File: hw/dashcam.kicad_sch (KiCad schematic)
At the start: 1 part, among them U1 AM6254ATCGHAALW

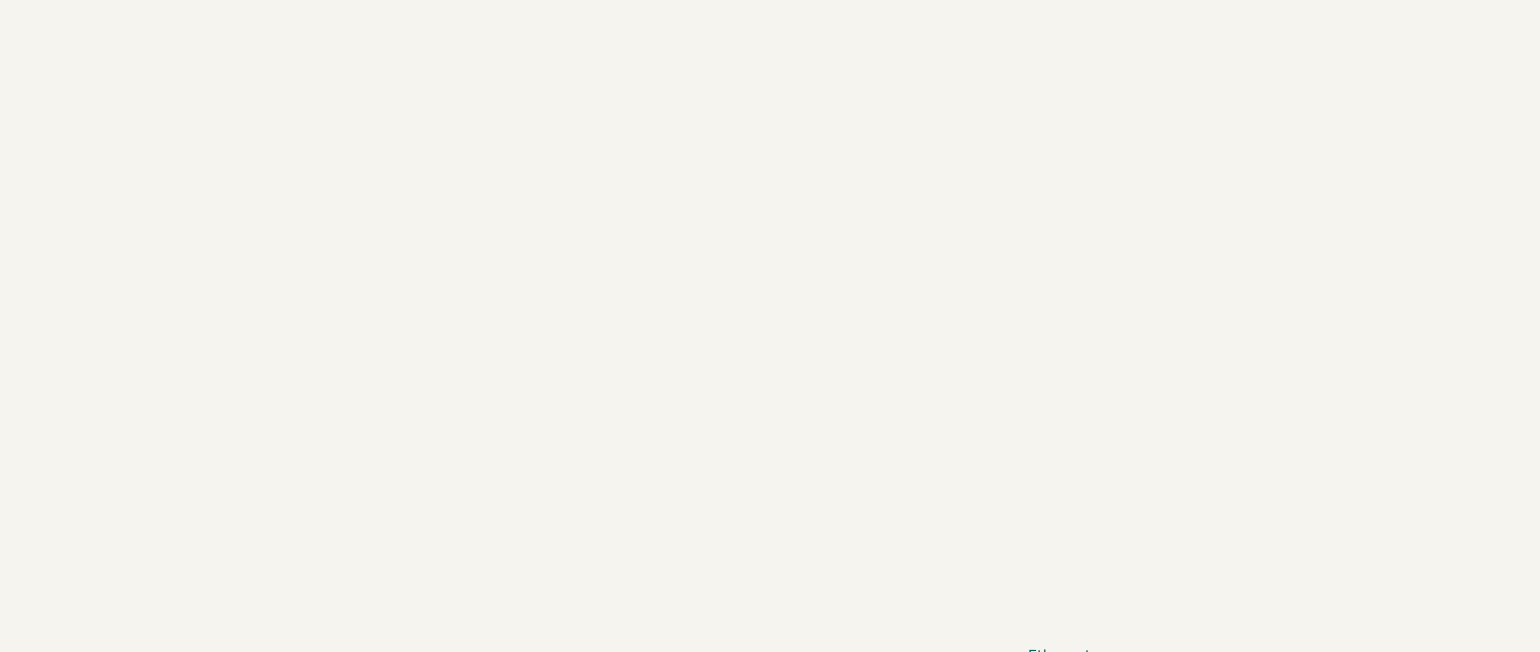
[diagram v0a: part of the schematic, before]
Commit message: Folder rest. and rtc design with OSC yet to be connected
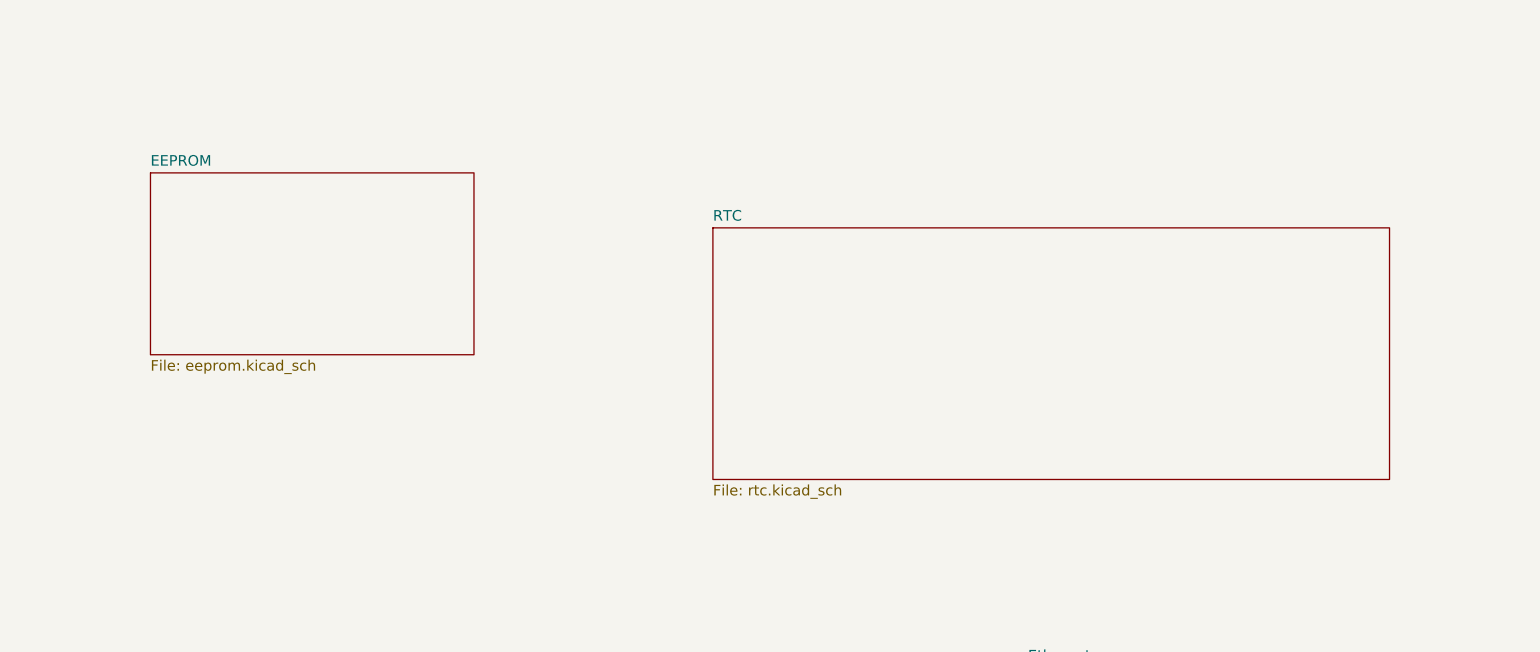
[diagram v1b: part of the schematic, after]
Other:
- added sheet EEPROM (eeprom.kicad_sch)
- added sheet RTC (rtc.kicad_sch)
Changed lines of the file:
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@@
+	)
+	(sheet
+		(at 245.364 99.568)
+		(size 81.28 30.226)
+		(exclude_from_sim no)
+		(in_bom yes)
+		(on_board yes)
+		(dnp no)
+		(fields_autoplaced yes)
+		(stroke
+			(width 0.1524)
+			(type solid)
+		)
+		(fill
+			(color 0 0 0 0.0000)
+		)
+		(property "Sheetname" "RTC"
+			(at 245.364 98.8564 0)
+			(effects
+				(font
+					(size 1.27 1.27)
+				)
+				(justify left bottom)
+			)
+		)
+		(property "Sheetfile" "rtc.kicad_sch"
+			(at 245.364 130.3786 0)
+			(effects
+				(font
+					(size 1.27 1.27)
+				)
+				(justify left top)
+			)
+		)
+		(instances
+			(project "dashcam"
+				(path "/30d6913c-7aa4-4f56-9882-2ba08f7e2cce"
+					(page "15")
+				)
+			)
+		)
 	)
 	(sheet
@@
 				)
 			)
+		)
+	)
+	(sheet
+		(at 177.8 92.964)
+		(size 38.862 21.844)
+		(exclude_from_sim no)
+		(in_bom yes)
+		(on_board yes)
+		(dnp no)
+		(fields_autoplaced yes)
+		(stroke
+			(width 0.1524)
+			(type solid)
+		)
+		(fill
+			(color 0 0 0 0.0000)
+		)
+		(property "Sheetname" "EEPROM"
+			(at 177.8 92.2524 0)
+			(effects
+				(font
+					(size 1.27 1.27)
+				)
+				(justify left bottom)
+			)
+		)
+		(property "Sheetfile" "eeprom.kicad_sch"
+			(at 177.8 115.3926 0)
+			(effects
+				(font
+					(size 1.27 1.27)
+				)
+				(justify left top)
+			)
+		)
+		(instances
+			(project "dashcam"
+				(path "/30d6913c-7aa4-4f56-9882-2ba08f7e2cce"
+					(page "13")
+				)
+			)

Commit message: Ethernet...
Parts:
- removed unit 6 of U1
- added X2: SC-20S32.768kHz20PPM9pF, pepy_sym_lib:[Crystal]Seiko SC-20S,32.768kHz,20PPM,9pF, symbol pepy_sym_lib:[Crystal]Seiko SC-20S,32.768kHz,20PPM,9pF
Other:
- added sheet LTE (LTE.kicad_sch)
- added sheet ddr (ddr.kicad_sch)

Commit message: WIP SIM module
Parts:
- added R1: RC0201FR-0733RL, pepy_sym_lib:[RES_SMD_0201_0603Metric], symbol pepy_sym_lib:[RES_SMD_0201_0603Metric]YAGEO RC0201FR-0733RL
- renumbered X2 to X1
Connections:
- net at U1.B8 (MCU_SPI0_CS1): now also R1.1
- new net MCU_OBSCLK0: R1.2
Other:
- note added: "CLK to PHY (25MHz) [MCU Domain Observation clock output for test and debug purposes only]"
- moved on the sheet: U1R
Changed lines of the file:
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@@
 		(rev "v0.1")
 	)
+	(text "CLK to PHY (25MHz) [MCU Domain Observation clock\noutput for test and debug purposes only]"
+		(exclude_from_sim no)
+		(at 163.83 44.704 0)
+		(effects
+			(font
+				(size 0.6 0.6)
+			)
+			(justify left)
+		)
+	)
 	(no_connect
 		(at 558.8 -191.77)
@@
 		(at 558.8 -194.31)
 	)
+	(wire
+		(pts
+			(xy 143.51 44.45) (xy 147.32 44.45)
+		)
+		(stroke
+			(width 0)
+			(type default)
+		)
+	)
+	(wire
+		(pts
+			(xy 138.43 44.45) (xy 137.16 44.45)
+		)
+		(stroke
+			(width 0)
+			(type default)
+		)
+	)
+	(global_label "MCU_OBSCLK0"
+		(shape output)
+		(at 147.32 44.45 0)
+		(fields_autoplaced yes)
+		(effects
+			(font
+				(size 1.27 1.27)
+			)
+			(justify left)
+		)
+		(property "Intersheetrefs" "${INTERSHEET_REFS}"
+			(at 163.9123 44.45 0)
+			(effects
+				(font
+					(size 1.27 1.27)
+				)
+				(justify left)
+				(hide yes)
+			)
+		)
+	)
 	(symbol
 		(lib_id "pepy_sym_lib:[CPU]Texas Instruments AM6254ATCGHAALW")
@@
 	)
 	(symbol
+		(lib_id "pepy_sym_lib:[RES_SMD_0201_0603Metric]YAGEO RC0201FR-0733RL")
+		(at 140.97 44.45 0)
+		(unit 1)
+		(exclude_from_sim no)
+		(in_bom yes)
+		(on_board yes)
+		(dnp no)
+		(property "Reference" "R1"
+			(at 140.9699 42.8396 0)
+			(do_not_autoplace yes)
+			(effects
+				(font
+					(size 1.27 1.27)
+				)
+			)
+		)
+		(property "Value" "RC0201FR-0733RL"
+			(at 141.224 62.738 0)
+			(effects
+				(font
+					(size 1.27 1.27)
+				)
+				(hide yes)
+			)
+		)
+		(property "Footprint" "pepy_sym_lib:[RES_SMD_0201_0603Metric]"
+			(at 140.97 50.8 0)
+			(effects
+				(font
+					(size 1.27 1.27)
+				)
+				(hide yes)
+			)
+		)
+		(property "Datasheet" "https://www.lcsc.com/product-detail/Chip-Resistor-Surface-Mount_YAGEO-RC0201FR-0733RL_C295794.html"
+			(at 140.97 53.34 0)
+			(effects
+				(font
+					(size 1.27 1.27)
+				)
+				(hide yes)
+			)
+		)
+		(property "Description" "50mW Thick Film Resistors 25V ±1% ±200ppm/℃ 33Ω 0201 Chip Resistor - Surface Mount ROHS"
+			(at 142.494 58.166 0)
+			(effects
+				(font
+					(size 1.27 1.27)
+				)
+				(hide yes)
+			)
+		)
+		(property "LCSC Part" "C295794"
+			(at 140.97 55.88 0)
+			(effects
+				(font
+					(size 1.27 1.27)
+				)
+				(hide yes)
+			)
+		)
+		(property "Manufacturer" "YAGEO"
+			(at 141.732 60.198 0)
+			(effects
+				(font
+					(size 1.27 1.27)
+				)
+				(hide yes)
+			)
+		)
+		(property "Nvalue" "33R"
+			(at 140.97 46.1301 0)
+			(do_not_autoplace yes)
+			(effects
+				(font
+					(size 1.27 1.27)
+				)
+			)
+		)
+		(property "Package" "0201"
+			(at 140.97 48.26 0)
+			(effects
+				(font
+					(size 1.27 1.27)
+				)
+				(hide yes)
+			)
+		)
+		(property "Tolerance" "1%"
+			(at 140.97 64.516 0)
+			(effects
+				(font
+					(size 1.27 1.27)
+				)
+				(hide yes)
+			)
+		)
+		(pin "1"
+		)
+		(pin "2"
+		)
+		(instances
+			(project "dashcam"
+				(path "/30d6913c-7aa4-4f56-9882-2ba08f7e2cce"
+					(reference "R1")
+					(unit 1)
+				)
+			)
+		)
+	)
+	(symbol
 		(lib_id "pepy_sym_lib:[CPU]Texas Instruments AM6254ATCGHAALW")
 		(at 772.16 370.84 0)
@@
 		(dnp no)
 		(fields_autoplaced yes)
-		(property "Reference" "X2"
+		(property "Reference" "X1"
 			(at 167.64 140.97 0)
 			(effects
@@
 			(project ""
 				(path "/30d6913c-7aa4-4f56-9882-2ba08f7e2cce"
-					(reference "X2")
+					(reference "X1")
 					(unit 1)
 				)
@@
 	(symbol
 		(lib_id "pepy_sym_lib:[CPU]Texas Instruments AM6254ATCGHAALW")
-		(at 651.51 -236.22 0)
+		(at 111.76 76.2 0)
 		(unit 18)
 		(exclude_from_sim no)
@@
 		(fields_autoplaced yes)
 		(property "Reference" "U1"
-			(at 650.875 -290.83 0)
+			(at 111.125 21.59 0)
 			(effects
 				(font
@@
 		)
 		(property "Value" "AM6254ATCGHAALW"
-			(at 650.875 -288.29 0)
+			(at 111.125 24.13 0)
 			(effects
 				(font
@@
 		)
 		(property "Footprint" "pepy_sym_lib:[CPU]Texas Instruments AM6254ATCGHAALW"
-			(at 651.256 -229.362 0)
+			(at 111.506 83.058 0)
 			(effects
 				(font
@@
 		)
 		(property "Datasheet" "https://www.ti.com/lit/ds/symlink/am625.pdf?ts=1740314582358&ref_url=https%253A%252F%252Fwww.ti.com%252Fmicrocontrollers-mcus-processors%252Farm-based-processors%252Fproducts.html"
-			(at 651.51 -224.536 0)
+			(at 111.76 87.884 0)
 			(effects
 				(font
@@
 		)
 		(property "Description" "1400MHz FCCSP(ALW)-425 Microcontrollers (MCU/MPU/SOC) ROHS"
-			(at 651.256 -222.25 0)
+			(at 111.506 90.17 0)
 			(effects
 				(font
@@
 		)
 		(property "LCSC Part" "C5218241"
-			(at 651.256 -226.822 0)
+			(at 111.506 85.598 0)
 			(effects
 				(font
@@
 		)
 		(property "Manufacturer" "Texas Instruments"
-			(at 651.002 -219.964 0)
+			(at 111.252 92.456 0)
 			(effects
 				(font
